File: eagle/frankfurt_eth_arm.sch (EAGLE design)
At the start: 83 parts, among them IC1 STM32F103C6T7A, IC2 ENC28J60-SO, IC3 SN65HVD232, IC4 LM2575S, IC5 11AA02E48, IC6 MCP23A256, IC7 AT45DB041D, J2 A00-108-220-450, Q1 8 MHz, Q2 25 MHz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

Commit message: Routed
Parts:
- removed JTAG: (no value), con-lstb:MA10-2
- removed R30, R31: 10K, rcl:R-EU_R0805
- added J1: (no value), con-lstb:MA05-2
- added UART1: 22-23-2041, con-molex:22-23-2041
- R29: value 47K -> 10K
- R3: value 1K -> 10K
- renumbered SJ1 to J3, SV1 to BOOT0, SV2 to BOOT1
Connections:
- net N$18 renamed _BOOT0
- net N$23 renamed BOOT0
- net N$26 renamed _BOOT1
- removed net INT0: IC2.INT
- removed net INT1: IC2.WOL
- removed net N$30: IC1.PA11
- removed net N$31: IC1.PA12
- removed net N$32: JTAG.12, R31.2
- removed net N$36: JTAG.18, R30.2
- removed net N$38: JTAG.20, R29.2
- removed net N$4: R3.2
- removed net N$6: C7.2, R4.1, S1.P
- removed net REST: C5.1, IC1.NRST, R2.1
- removed net SWCK: IC1.PA14
- removed net SWDIO: IC1.PA13
- removed net SWO: IC1.PB3
- removed net TCK: JTAG.10, R27.1
- removed net TDO: JTAG.14, R28.1
- removed net TMS: JTAG.8, R26.1
- new net CANRXD: IC1.PA11, IC3>NAME.RXD
- new net CANTXD: IC1.PA12, IC3>NAME.TXD
- new net ETH_INT0: IC1.PB8, IC2.INT, R24.2
- new net ETH_INT1: IC1.PB9, IC2.WOL, R29.2
- new net INIT: IC1.PB13, R3.2
- new net INITSW: C7.2, IC1.PB14, R4.1, S1.P
- new net SWDIO/TMS: IC1.PA13, J1.2, R25.1
- new net TCK/SWCK: IC1.PA14, J1.4, R26.1
- new net TDO/SWO: IC1.PB3, J1.6, R27.1
- new net UART1_RX: IC1.PA10, UART1-2.S
- new net UART1_TX: IC1.PA9, UART1-3.S
- net CANL: now also IC3>NAME.VREF
- net ETH_CS: now also IC1.PA4
- net ETH_RESET: now also IC1.PB15
- net EUI48: now also IC1.PB11
- net GND: now also J1.3, J1.5, J1.7, J1.9, UART1-4.S; no longer JTAG.11, JTAG.13, JTAG.15, JTAG.17, JTAG.19, JTAG.3, JTAG.5, JTAG.7, JTAG.9, R29.1, R30.1, R31.1
- net MISO: now also IC1.PA6
- net MOSI: now also IC1.PA7
- net RAM_CS: now also IC1.PB10
- net ROM_CS1: now also IC1.PA3
- net RST: now also C5.1, IC1.NRST, R2.1; no longer JTAG.16
- net SCK: now also IC1.PA5
- net TDI: now also J1.8, R28.1; no longer JTAG.6, R25.1
- net TRST: now also J1.10; no longer JTAG.4, R24.1
- net VCC: now also J1.1, R24.1, R29.1, UART1-1.S; no longer JTAG.1, JTAG.2, R24.2
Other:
- note added: "JTAG 10-pin"
- moved on the sheet: IC3

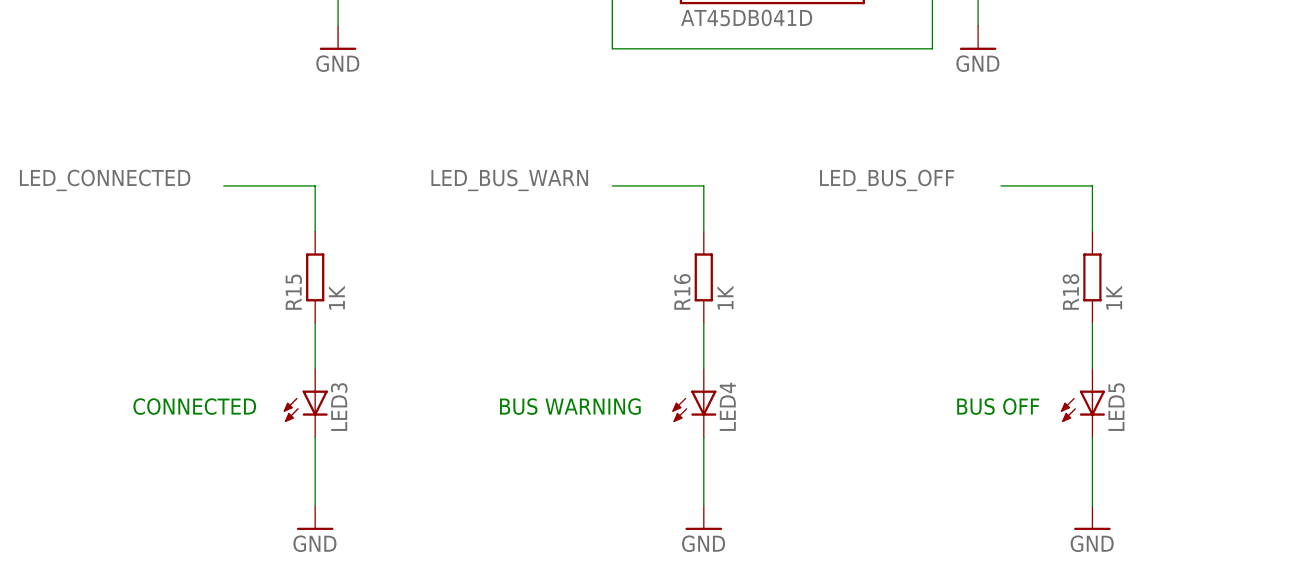
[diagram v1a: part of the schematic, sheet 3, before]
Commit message: Removed extra status LED's
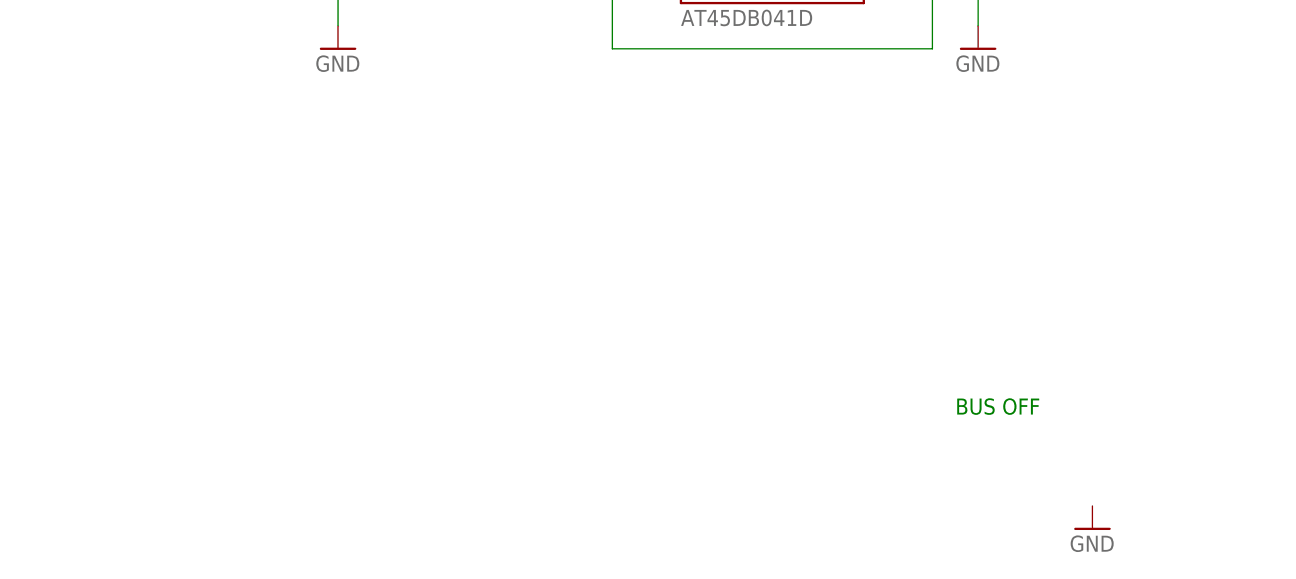
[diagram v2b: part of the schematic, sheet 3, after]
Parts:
- removed LED3, LED4, LED5: (no value), led:LEDCHIP-LED0805
- removed R15, R16, R18: 1K, rcl:R-EU_R0805
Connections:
- removed net LED_BUS_OFF: R18.2
- removed net LED_CONNECTED: R15.2
- removed net N$14: LED3.A, R15.1
- removed net N$21: LED4.A, R16.1
- removed net N$24: LED5.A, R18.1
- net GND: no longer LED3.C, LED4.C, LED5.C
- net LED_BUS_WARN: now also IC1.PB12; no longer R16.2
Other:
- note removed: "BUS WARNING"
- note removed: "CONNECTED"
- moved on the sheet: BOOT1, R21
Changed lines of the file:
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@@
 <part name="GND37" library="SUPPLY1" deviceset="GND" device=""/>
 <part name="C16" library="rcl" deviceset="C-EU" device="C0805" value="0.1uF"/>
-<part name="GND35" library="SUPPLY1" deviceset="GND" device=""/>
-<part name="R15" library="rcl" deviceset="R-EU_" device="R0805" value="1K"/>
-<part name="LED3" library="led" deviceset="LED" device="CHIP-LED0805"/>
-<part name="GND36" library="SUPPLY1" deviceset="GND" device=""/>
-<part name="R16" library="rcl" deviceset="R-EU_" device="R0805" value="1K"/>
-<part name="LED4" library="led" deviceset="LED" device="CHIP-LED0805"/>
 <part name="GND38" library="SUPPLY1" deviceset="GND" device=""/>
-<part name="R18" library="rcl" deviceset="R-EU_" device="R0805" value="1K"/>
-<part name="LED5" library="led" deviceset="LED" device="CHIP-LED0805"/>
 <part name="IC1" library="STM32F103C6T7A" deviceset="STM32F103C6T7A" device=""/>
 <part name="GND20" library="SUPPLY1" deviceset="GND" device=""/>
@@
 <instance part="R20" gate="G$1" x="71.12" y="147.32" rot="R90"/>
 <instance part="P+17" gate="VCC" x="66.04" y="152.4"/>
-<instance part="BOOT1" gate="G$1" x="147.32" y="137.16"/>
-<instance part="GND40" gate="1" x="160.02" y="127"/>
-<instance part="R21" gate="G$1" x="160.02" y="147.32" rot="R90"/>
-<instance part="P+18" gate="VCC" x="154.94" y="157.48"/>
+<instance part="BOOT1" gate="G$1" x="147.32" y="129.54"/>
+<instance part="GND40" gate="1" x="160.02" y="119.38"/>
+<instance part="R21" gate="G$1" x="162.56" y="137.16" rot="R90"/>
+<instance part="P+18" gate="VCC" x="154.94" y="142.24"/>
 <instance part="P+20" gate="VCC" x="27.94" y="246.38"/>
 <instance part="C15" gate="G$1" x="27.94" y="220.98"/>
@@
 <segment>
 <pinref part="BOOT1" gate="G$1" pin="3"/>
-<wire x1="154.94" y1="139.7" x2="154.94" y2="154.94" width="0.1524" layer="91"/>
+<wire x1="154.94" y1="132.08" x2="154.94" y2="139.7" width="0.1524" layer="91"/>
 <pinref part="P+18" gate="VCC" pin="VCC"/>
 </segment>
@@
 <pinref part="BOOT1" gate="G$1" pin="1"/>
 <pinref part="GND40" gate="1" pin="GND"/>
-<wire x1="154.94" y1="134.62" x2="160.02" y2="134.62" width="0.1524" layer="91"/>
-<wire x1="160.02" y1="134.62" x2="160.02" y2="129.54" width="0.1524" layer="91"/>
+<wire x1="154.94" y1="127" x2="160.02" y2="127" width="0.1524" layer="91"/>
+<wire x1="160.02" y1="127" x2="160.02" y2="121.92" width="0.1524" layer="91"/>
 </segment>
 <segment>
@@
 <segment>
 <pinref part="IC1" gate="A" pin="PB2"/>
-<label x="149.86" y="182.88" size="1.778" layer="95"/>
+<label x="154.94" y="182.88" size="1.778" layer="95"/>
 <pinref part="R21" gate="G$1" pin="2"/>
-<wire x1="160.02" y1="182.88" x2="160.02" y2="152.4" width="0.1524" layer="91"/>
-<wire x1="134.62" y1="182.88" x2="160.02" y2="182.88" width="0.1524" layer="91"/>
+<wire x1="162.56" y1="182.88" x2="162.56" y2="142.24" width="0.1524" layer="91"/>
+<wire x1="134.62" y1="182.88" x2="162.56" y2="182.88" width="0.1524" layer="91"/>
 </segment>
 </net>
@@
 <pinref part="BOOT1" gate="G$1" pin="2"/>
 <pinref part="R21" gate="G$1" pin="1"/>
-<wire x1="154.94" y1="137.16" x2="160.02" y2="137.16" width="0.1524" layer="91"/>
-<wire x1="160.02" y1="137.16" x2="160.02" y2="142.24" width="0.1524" layer="91"/>
+<wire x1="154.94" y1="129.54" x2="162.56" y2="129.54" width="0.1524" layer="91"/>
+<wire x1="162.56" y1="129.54" x2="162.56" y2="132.08" width="0.1524" layer="91"/>
 </segment>
 </net>
@@
 <pinref part="IC1" gate="A" pin="PA3"/>
 <wire x1="134.62" y1="223.52" x2="139.7" y2="223.52" width="0.1524" layer="91"/>
+</segment>
+</net>
+<net name="LED_BUS_WARN" class="0">
+<segment>
+<pinref part="IC1" gate="A" pin="PB12"/>
+<wire x1="134.62" y1="157.48" x2="139.7" y2="157.48" width="0.1524" layer="91"/>
+<label x="139.7" y="157.48" size="1.778" layer="95"/>
 </segment>
 </net>
@@
 <sheet>
 <plain>
-<text x="58.42" y="162.56" size="1.778" layer="91">CONNECTED</text>
-<text x="99.06" y="162.56" size="1.778" layer="91">BUS WARNING</text>
 <text x="149.86" y="162.56" size="1.778" layer="91">BUS OFF</text>
 </plain>
@@
 <instance part="GND37" gate="1" x="81.28" y="203.2"/>
 <instance part="C16" gate="G$1" x="81.28" y="213.36" rot="R180"/>
-<instance part="GND35" gate="1" x="78.74" y="149.86"/>
-<instance part="R15" gate="G$1" x="78.74" y="177.8" rot="R90"/>
-<instance part="LED3" gate="G$1" x="78.74" y="165.1"/>
-<instance part="GND36" gate="1" x="121.92" y="149.86"/>
-<instance part="R16" gate="G$1" x="121.92" y="177.8" rot="R90"/>
-<instance part="LED4" gate="G$1" x="121.92" y="165.1"/>
 <instance part="GND38" gate="1" x="165.1" y="149.86"/>
-<instance part="R18" gate="G$1" x="165.1" y="177.8" rot="R90"/>
-<instance part="LED5" gate="G$1" x="165.1" y="165.1"/>
 </instances>
 <busses>
@@
 <pinref part="GND37" gate="1" pin="GND"/>
 <wire x1="81.28" y1="210.82" x2="81.28" y2="205.74" width="0.1524" layer="91"/>
-</segment>
-<segment>
-<wire x1="78.74" y1="160.02" x2="78.74" y2="152.4" width="0.1524" layer="91"/>
-<pinref part="GND35" gate="1" pin="GND"/>
-<pinref part="LED3" gate="G$1" pin="C"/>
-</segment>
-<segment>
-<wire x1="121.92" y1="160.02" x2="121.92" y2="152.4" width="0.1524" layer="91"/>
-<pinref part="GND36" gate="1" pin="GND"/>
-<pinref part="LED4" gate="G$1" pin="C"/>
-</segment>
-<segment>
-<wire x1="165.1" y1="160.02" x2="165.1" y2="152.4" width="0.1524" layer="91"/>
-<pinref part="GND38" gate="1" pin="GND"/>
-<pinref part="LED5" gate="G$1" pin="C"/>
 </segment>
 </net>
@@
 </segment>
 </net>
-<net name="LED_CONNECTED" class="0">
-<segment>
-<wire x1="78.74" y1="187.96" x2="78.74" y2="182.88" width="0.1524" layer="91"/>
-<pinref part="R15" gate="G$1" pin="2"/>
-<wire x1="78.74" y1="187.96" x2="68.58" y2="187.96" width="0.1524" layer="91"/>
-<label x="45.72" y="187.96" size="1.778" layer="95"/>
-</segment>
-</net>
-<net name="N$14" class="0">
-<segment>
-<wire x1="78.74" y1="167.64" x2="78.74" y2="172.72" width="0.1524" layer="91"/>
-<pinref part="R15" gate="G$1" pin="1"/>
-<pinref part="LED3" gate="G$1" pin="A"/>
-</segment>
-</net>
-<net name="LED_BUS_WARN" class="0">
-<segment>
-<wire x1="121.92" y1="187.96" x2="121.92" y2="182.88" width="0.1524" layer="91"/>
-<pinref part="R16" gate="G$1" pin="2"/>
-<wire x1="121.92" y1="187.96" x2="111.76" y2="187.96" width="0.1524" layer="91"/>
-<label x="91.44" y="187.96" size="1.778" layer="95"/>
-</segment>
-</net>
-<net name="N$21" class="0">
-<segment>
-<wire x1="121.92" y1="167.64" x2="121.92" y2="172.72" width="0.1524" layer="91"/>
-<pinref part="R16" gate="G$1" pin="1"/>
-<pinref part="LED4" gate="G$1" pin="A"/>
-</segment>
-</net>
-<net name="LED_BUS_OFF" class="0">
-<segment>
-<wire x1="165.1" y1="187.96" x2="165.1" y2="182.88" width="0.1524" layer="91"/>
-<pinref part="R18" gate="G$1" pin="2"/>
-<wire x1="165.1" y1="187.96" x2="154.94" y2="187.96" width="0.1524" layer="91"/>
-<label x="134.62" y="187.96" size="1.778" layer="95"/>
-</segment>
-</net>
-<net name="N$24" class="0">
-<segment>
-<wire x1="165.1" y1="167.64" x2="165.1" y2="172.72" width="0.1524" layer="91"/>
-<pinref part="R18" gate="G$1" pin="1"/>
-<pinref part="LED5" gate="G$1" pin="A"/>
-</segment>
-</net>

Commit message: edit text layer
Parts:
- removed Q1: 8 MHz, vscpcan:HC-49S
- added J5: TAMPER, con-molex:22-23-2021
- X1: value TAMPER -> 8 MHz; device con-molex:22-23-2021 -> vscpcan:HC-49S
- renumbered Q2 to X3
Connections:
- net GND: now also J5-2.S; no longer X1-2.S
- net N$2: now also X1.1; no longer Q1.1
- net N$27: now also J5-1.S; no longer X1-1.S
- net N$7: now also X1.2; no longer Q1.2
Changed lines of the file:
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@@
 <part name="C7" library="rcl" deviceset="C-EU" device="C0805" value="0.1uF"/>
 <part name="GND1" library="SUPPLY1" deviceset="GND" device=""/>
-<part name="Q1" library="vscpcan" deviceset="HC-49S" device="" value="8 MHz"/>
+<part name="X1" library="vscpcan" deviceset="HC-49S" device="" value="8 MHz"/>
 <part name="LED1" library="led" deviceset="LED" device="CHIP-LED0805"/>
 <part name="J4" library="con-lstb" deviceset="MA04-1" device=""/>
@@
 <part name="C10" library="rcl" deviceset="C-EU" device="C0805" value="18pF"/>
 <part name="C11" library="rcl" deviceset="C-EU" device="C0805" value="18pF"/>
-<part name="Q2" library="vscpcan" deviceset="HC-49S" device="" value="25 MHz"/>
+<part name="X3" library="vscpcan" deviceset="HC-49S" device="" value="25 MHz"/>
 <part name="GND24" library="SUPPLY1" deviceset="GND" device=""/>
 <part name="P+10" library="SUPPLY1" deviceset="VCC" device=""/>
@@
 <part name="GND32" library="SUPPLY1" deviceset="GND" device=""/>
 <part name="P+21" library="SUPPLY1" deviceset="VCC" device=""/>
-<part name="X1" library="con-molex" deviceset="22-23-2021" device="" value="TAMPER"/>
+<part name="J5" library="con-molex" deviceset="22-23-2021" device="" value="TAMPER"/>
 <part name="GND46" library="SUPPLY1" deviceset="GND" device=""/>
 <part name="R23" library="rcl" deviceset="R-EU_" device="R0805" value="10K"/>
@@
 <instance part="C7" gate="G$1" x="198.12" y="170.18" rot="R180"/>
 <instance part="GND1" gate="1" x="198.12" y="162.56"/>
-<instance part="Q1" gate="G$1" x="33.02" y="177.8"/>
+<instance part="X1" gate="G$1" x="33.02" y="177.8"/>
 <instance part="LED1" gate="G$1" x="170.18" y="177.8"/>
 <instance part="J4" gate="1" x="259.08" y="177.8" rot="R90"/>
@@
 <instance part="GND32" gate="1" x="10.16" y="185.42"/>
 <instance part="P+21" gate="VCC" x="10.16" y="213.36"/>
-<instance part="X1" gate="-1" x="7.62" y="175.26"/>
-<instance part="X1" gate="-2" x="7.62" y="172.72"/>
+<instance part="J5" gate="-1" x="7.62" y="175.26"/>
+<instance part="J5" gate="-2" x="7.62" y="172.72"/>
 <instance part="GND46" gate="1" x="5.08" y="167.64"/>
 <instance part="R23" gate="G$1" x="10.16" y="205.74" rot="R90"/>
@@
 <segment>
 <pinref part="GND46" gate="1" pin="GND"/>
-<pinref part="X1" gate="-2" pin="S"/>
+<pinref part="J5" gate="-2" pin="S"/>
 <wire x1="5.08" y1="170.18" x2="5.08" y2="172.72" width="0.1524" layer="91"/>
 </segment>
@@
 <junction x="27.94" y="177.8"/>
 <pinref part="C4" gate="G$1" pin="2"/>
-<pinref part="Q1" gate="G$1" pin="1"/>
+<pinref part="X1" gate="G$1" pin="1"/>
 <pinref part="IC1" gate="A" pin="PD0-OSC_IN"/>
 <wire x1="27.94" y1="193.04" x2="83.82" y2="193.04" width="0.1524" layer="91"/>
@@
 <junction x="38.1" y="177.8"/>
 <pinref part="C6" gate="G$1" pin="2"/>
-<pinref part="Q1" gate="G$1" pin="2"/>
+<pinref part="X1" gate="G$1" pin="2"/>
 <pinref part="IC1" gate="A" pin="PD1-OSC_OUT"/>
 <wire x1="38.1" y1="187.96" x2="38.1" y2="190.5" width="0.1524" layer="91"/>
@@
 <wire x1="71.12" y1="198.12" x2="10.16" y2="198.12" width="0.1524" layer="91"/>
 <junction x="10.16" y="198.12"/>
-<pinref part="X1" gate="-1" pin="S"/>
+<pinref part="J5" gate="-1" pin="S"/>
 <wire x1="5.08" y1="175.26" x2="5.08" y2="198.12" width="0.1524" layer="91"/>
 <wire x1="5.08" y1="198.12" x2="10.16" y2="198.12" width="0.1524" layer="91"/>
@@
 <attribute name="VALUE" x="343.916" y="83.439" size="1.778" layer="96" rot="R180"/>
 </instance>
-<instance part="Q2" gate="G$1" x="330.2" y="91.44"/>
+<instance part="X3" gate="G$1" x="330.2" y="91.44"/>
 <instance part="GND24" gate="1" x="307.34" y="137.16"/>
 <instance part="P+10" gate="VCC" x="281.94" y="167.64"/>
@@
 <junction x="325.12" y="91.44"/>
 <pinref part="C10" gate="G$1" pin="2"/>
-<pinref part="Q2" gate="G$1" pin="1"/>
+<pinref part="X3" gate="G$1" pin="1"/>
 <pinref part="IC2" gate="G$1" pin="OSC2"/>
 <wire x1="309.88" y1="101.6" x2="325.12" y2="101.6" width="0.1524" layer="91"/>
@@
 <junction x="335.28" y="91.44"/>
 <pinref part="C11" gate="G$1" pin="2"/>
-<pinref part="Q2" gate="G$1" pin="2"/>
+<pinref part="X3" gate="G$1" pin="2"/>
 <pinref part="IC2" gate="G$1" pin="OSC1"/>
 <wire x1="309.88" y1="104.14" x2="335.28" y2="104.14" width="0.1524" layer="91"/>

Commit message: Updated rev texts
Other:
- note added: "ARM version"
- note added: "Frankfurt Eth"
- note removed: "Ethernet"
- note removed: "Expansion"
- note removed: "Odessa"
- note removed: "http://www.grodansparadis.com"
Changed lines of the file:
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@@
 <text x="200.66" y="175.26" size="1.778" layer="91">Horizontal type</text>
 <text x="378.46" y="7.62" size="1.778" layer="91">A</text>
-<text x="289.56" y="27.94" size="5.08" layer="91">Odessa</text>
+<text x="289.56" y="27.94" size="5.08" layer="91">Frankfurt Eth</text>
 <text x="365.76" y="25.4" size="1.778" layer="91">http://www.vscp.org</text>
-<text x="289.56" y="25.4" size="1.778" layer="91">Expansion</text>
+<text x="289.56" y="25.4" size="1.778" layer="91">ARM version</text>
 <text x="287.02" y="241.3" size="1.778" layer="91">Input voltage</text>
 <text x="287.02" y="238.76" size="1.778" layer="91">+7V DC - +28V DC</text>
@@
 <sheet>
 <plain>
-<text x="292.1" y="17.78" size="1.778" layer="91">Ethernet</text>
 <text x="375.92" y="2.54" size="1.778" layer="91">Rev A</text>
-<text x="292.1" y="15.24" size="1.778" layer="91">http://www.grodansparadis.com</text>
+<text x="289.56" y="15.24" size="5.08" layer="91">Frankfurt Eth</text>
+<text x="289.56" y="10.16" size="1.778" layer="91">http://www.vscp.org</text>
+<text x="289.56" y="12.7" size="1.778" layer="91">ARM version</text>
 </plain>
 <instances>
@@
 <plain>
 <text x="149.86" y="162.56" size="1.778" layer="91">BUS OFF</text>
+<text x="378.46" y="5.08" size="1.778" layer="91">A</text>
+<text x="292.1" y="15.24" size="5.08" layer="91">Frankfurt Eth</text>
+<text x="292.1" y="10.16" size="1.778" layer="91">http://www.vscp.org</text>
+<text x="292.1" y="12.7" size="1.778" layer="91">ARM version</text>
 </plain>
 <instances>
